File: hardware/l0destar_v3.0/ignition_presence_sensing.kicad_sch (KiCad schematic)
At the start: 5 parts

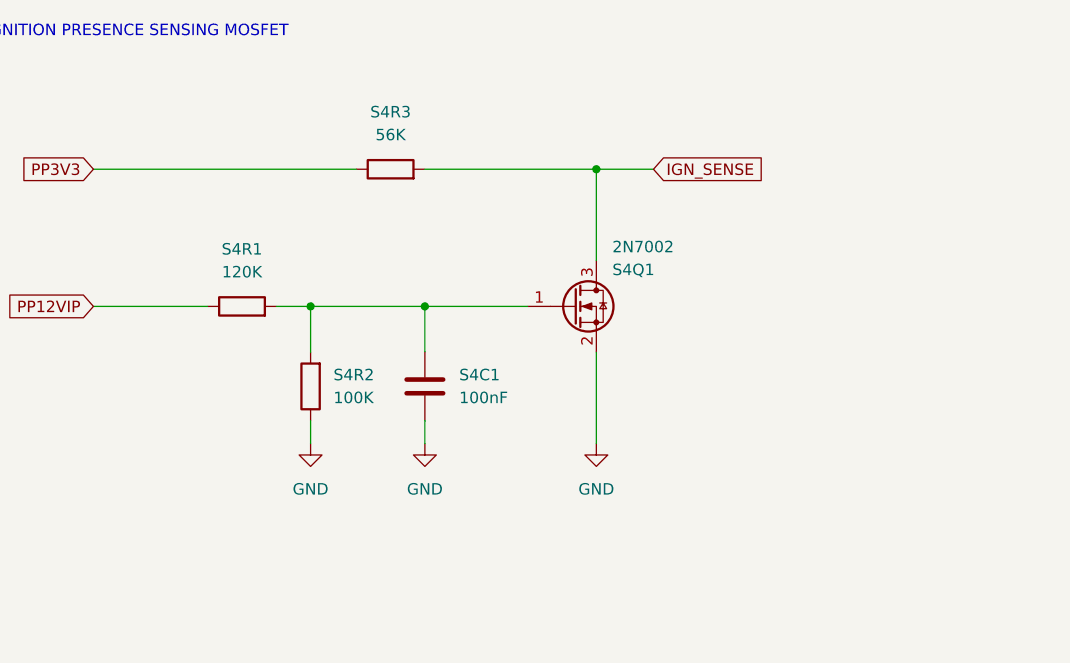
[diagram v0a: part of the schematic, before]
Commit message: updated v3.0 part specifications and added to the schematics
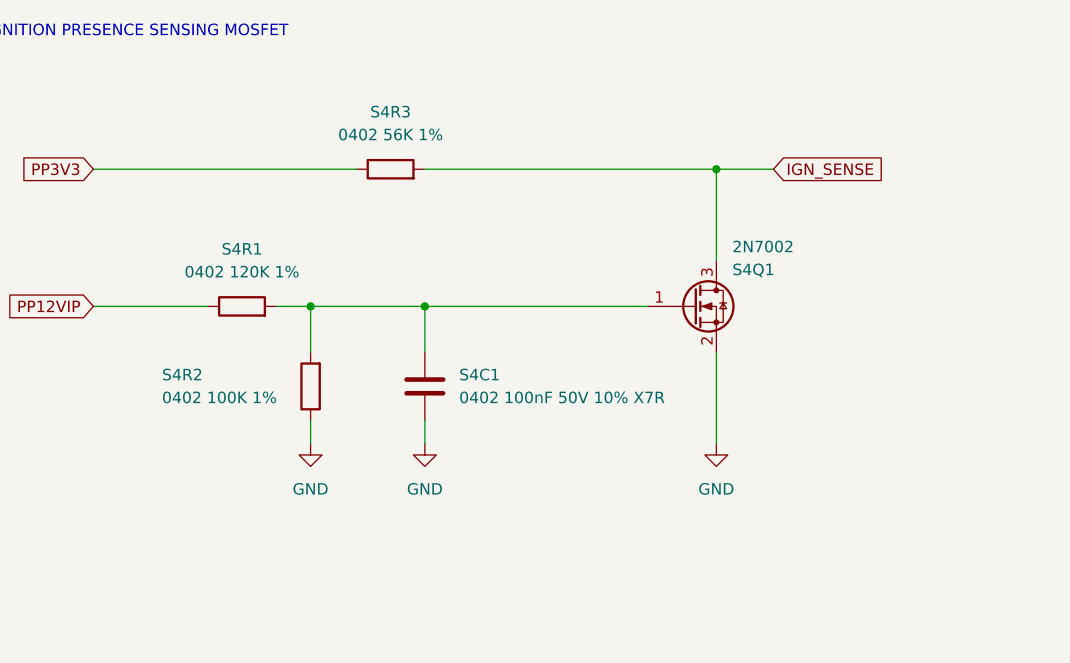
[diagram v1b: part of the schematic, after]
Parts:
- S4C1: value 100nF -> 0402 100nF 50V 10% X7R
- S4R1: value 120K -> 0402 120K 1%
- S4R2: value 100K -> 0402 100K 1%
- S4R3: value 56K -> 0402 56K 1%
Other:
- moved on the sheet: S4Q1
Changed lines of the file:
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@@
 	)
 	(junction
-		(at 95.25 38.1)
+		(at 108.585 38.1)
 		(diameter 0)
 		(color 0 0 0 0)
@@
 	(wire
 		(pts
-			(xy 95.25 68.58) (xy 95.25 58.42)
+			(xy 108.585 68.58) (xy 108.585 58.42)
 		)
 		(stroke
@@
 	(wire
 		(pts
-			(xy 76.2 38.1) (xy 95.25 38.1)
+			(xy 76.2 38.1) (xy 108.585 38.1)
 		)
 		(stroke
@@
 	(wire
 		(pts
-			(xy 95.25 38.1) (xy 95.25 48.26)
-		)
-		(stroke
-			(width 0)
-			(type default)
-		)
-	)
-	(wire
-		(pts
-			(xy 76.2 53.34) (xy 87.63 53.34)
+			(xy 108.585 38.1) (xy 108.585 48.26)
+		)
+		(stroke
+			(width 0)
+			(type default)
+		)
+	)
+	(wire
+		(pts
+			(xy 76.2 53.34) (xy 100.965 53.34)
 		)
 		(stroke
@@
 	(wire
 		(pts
-			(xy 95.25 38.1) (xy 101.6 38.1)
+			(xy 108.585 38.1) (xy 114.935 38.1)
 		)
 		(stroke
@@
 	(global_label "IGN_SENSE"
 		(shape input)
-		(at 101.6 38.1 0)
+		(at 114.935 38.1 0)
 		(fields_autoplaced yes)
 		(effects
@@
 		)
 		(property "Intersheetrefs" "${INTERSHEET_REFS}"
-			(at 114.8056 38.1 0)
+			(at 128.1406 38.1 0)
 			(hide yes)
 			(show_name no)
@@
 		(in_pos_files yes)
 		(dnp no)
-		(fields_autoplaced yes)
 		(property "Reference" "S4R2"
-			(at 66.04 60.9599 0)
+			(at 46.99 60.96 0)
 			(show_name no)
 			(do_not_autoplace no)
@@
 			)
 		)
-		(property "Value" "100K"
-			(at 66.04 63.4999 0)
+		(property "Value" "0402 100K 1%"
+			(at 46.99 63.5 0)
 			(show_name no)
 			(do_not_autoplace no)
@@
 			)
 		)
-		(property "Value" "56K"
+		(property "Value" "0402 56K 1%"
 			(at 72.39 34.29 90)
 			(show_name no)
@@
 	(symbol
 		(lib_id "Transistor_FET:2N7002")
-		(at 92.71 53.34 0)
+		(at 106.045 53.34 0)
 		(unit 1)
 		(body_style 1)
@@
 		(dnp no)
 		(property "Reference" "S4Q1"
-			(at 97.028 49.276 0)
+			(at 110.363 49.276 0)
 			(show_name no)
 			(do_not_autoplace no)
@@
 		)
 		(property "Value" "2N7002"
-			(at 97.028 46.736 0)
+			(at 110.363 46.736 0)
 			(show_name no)
 			(do_not_autoplace no)
@@
 		)
 		(property "Footprint" "Package_TO_SOT_SMD:SOT-23"
-			(at 97.79 55.245 0)
+			(at 111.125 55.245 0)
 			(hide yes)
 			(show_name no)
@@
 		)
 		(property "Datasheet" "https://www.onsemi.com/pub/Collateral/NDS7002A-D.PDF"
-			(at 97.79 57.15 0)
+			(at 111.125 57.15 0)
 			(hide yes)
 			(show_name no)
@@
 		)
 		(property "Description" "0.115A Id, 60V Vds, N-Channel MOSFET, SOT-23"
-			(at 92.71 53.34 0)
+			(at 106.045 53.34 0)
 			(hide yes)
 			(show_name no)
@@
 			)
 		)
-		(property "Value" "120K"
+		(property "Value" "0402 120K 1%"
 			(at 55.88 49.53 90)
 			(show_name no)
@@
 	(symbol
 		(lib_id "power:GND")
-		(at 95.25 68.58 0)
+		(at 108.585 68.58 0)
 		(unit 1)
 		(body_style 1)
@@
 		(fields_autoplaced yes)
 		(property "Reference" "#PWR010"
-			(at 95.25 74.93 0)
+			(at 108.585 74.93 0)
 			(hide yes)
 			(show_name no)
@@
 		)
 		(property "Value" "GND"
-			(at 95.25 73.66 0)
+			(at 108.585 73.66 0)
 			(show_name no)
 			(do_not_autoplace no)
@@
 		)
 		(property "Footprint" ""
-			(at 95.25 68.58 0)
+			(at 108.585 68.58 0)
 			(hide yes)
 			(show_name no)
@@
 		)
 		(property "Datasheet" ""
-			(at 95.25 68.58 0)
+			(at 108.585 68.58 0)
 			(hide yes)
 			(show_name no)
@@
 		)
 		(property "Description" "Power symbol creates a global label with name \"GND\" , ground"
-			(at 95.25 68.58 0)
+			(at 108.585 68.58 0)
 			(hide yes)
 			(show_name no)
@@
 			)
 		)
-		(property "Value" "100nF"
+		(property "Value" "0402 100nF 50V 10% X7R"
 			(at 80.01 63.4999 0)
 			(show_name no)

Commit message: fix discrepencies
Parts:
- S4R1: value 0402 120K 1% -> 0402 120K 5%
- S4R2: value 0402 100K 1% -> 0402 100K 5%
- S4R3: value 0402 56K 1% -> 0402 56K 5%
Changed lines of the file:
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@@
 			)
 		)
-		(property "Value" "0402 100K 1%"
+		(property "Value" "0402 100K 5%"
 			(at 46.99 63.5 0)
 			(show_name no)
@@
 			)
 		)
-		(property "Value" "0402 56K 1%"
+		(property "Value" "0402 56K 5%"
 			(at 72.39 34.29 90)
 			(show_name no)
@@
 			)
 		)
-		(property "Value" "0402 120K 1%"
+		(property "Value" "0402 120K 5%"
 			(at 55.88 49.53 90)
 			(show_name no)
